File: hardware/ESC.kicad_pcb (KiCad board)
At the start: 4 copper layers, 52 x 25 mm, 89 parts, among them J1 +, J10 +, J2 -, J3 +, J4 +, J5 +, J6 +, J7 Conn_01x03, J8 +, J9 +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

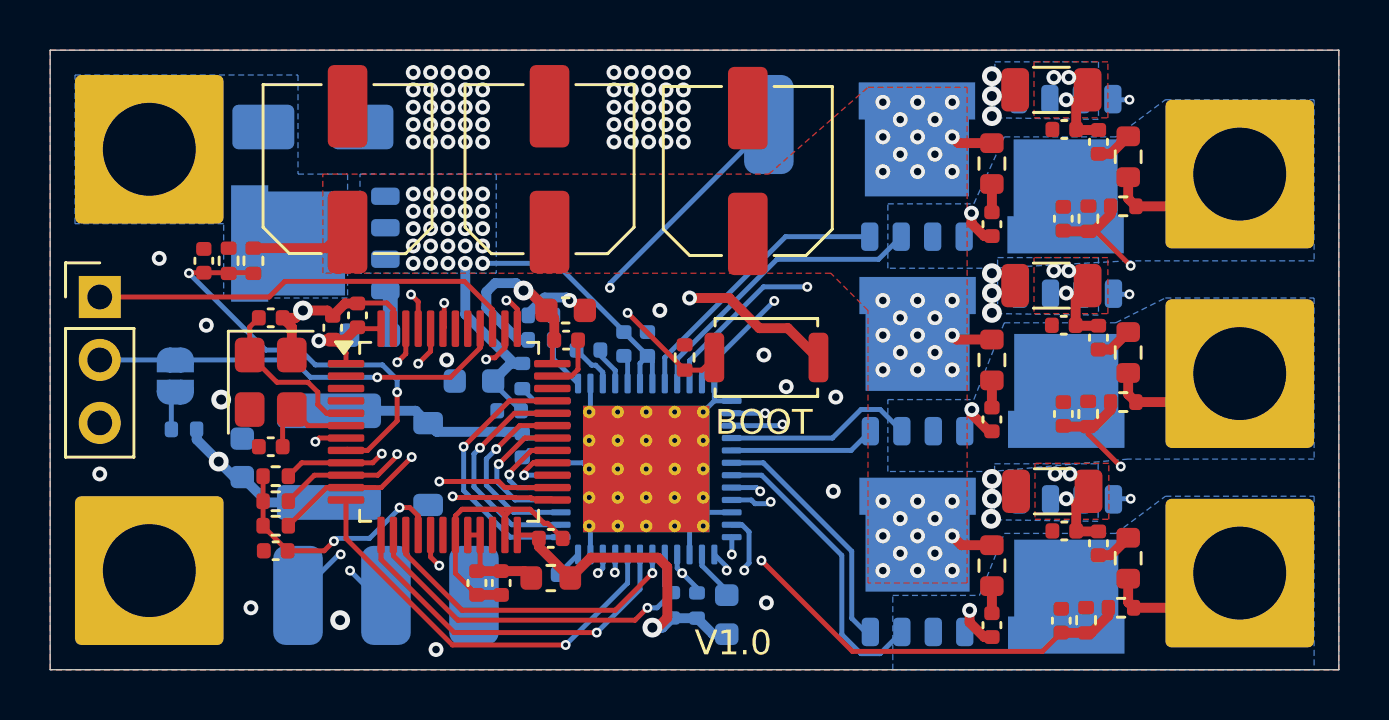
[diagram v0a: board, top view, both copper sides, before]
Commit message: increase via and trace size
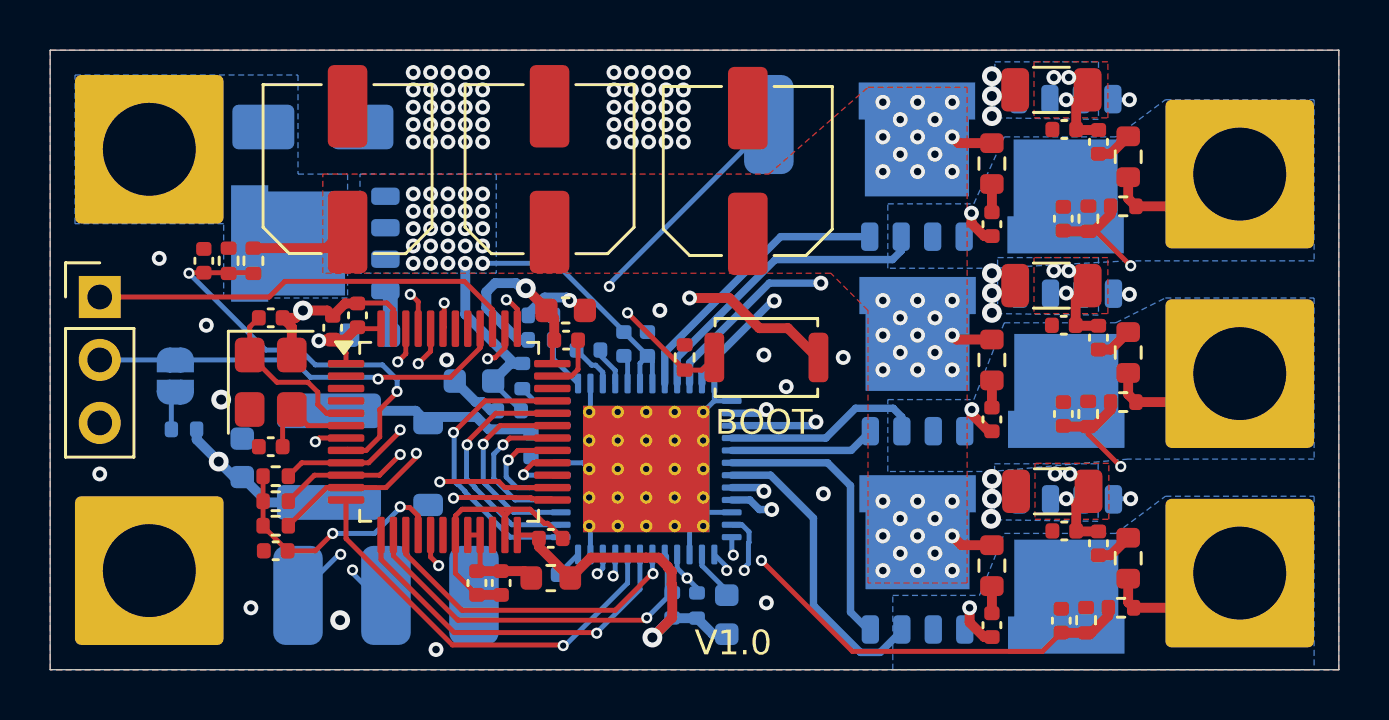
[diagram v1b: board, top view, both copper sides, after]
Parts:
- moved C7 0.35 mm to (157.4, 101.0)
- moved Q5 0.10 mm to (173.0, 105.7)
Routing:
- net /GLC: track 18.2 -> 21.0 mm
- net GND: track 46.6 -> 48.8 mm
- net /SPC: track 19.2 -> 17.0 mm
- net /GHC: track 10.1 -> 11.4 mm
- net /INHA: track 10.8 -> 11.7 mm
- net /SPA: track 23.4 -> 22.5 mm
- net +3.3V: track 51.7 -> 52.5 mm
- net /INLA: track 9.31 -> 10.00 mm
- net /INLB: track 6.22 -> 6.83 mm
- net /BGND: track 9.41 -> 10.0 mm
- net /INHB: track 7.74 -> 8.30 mm

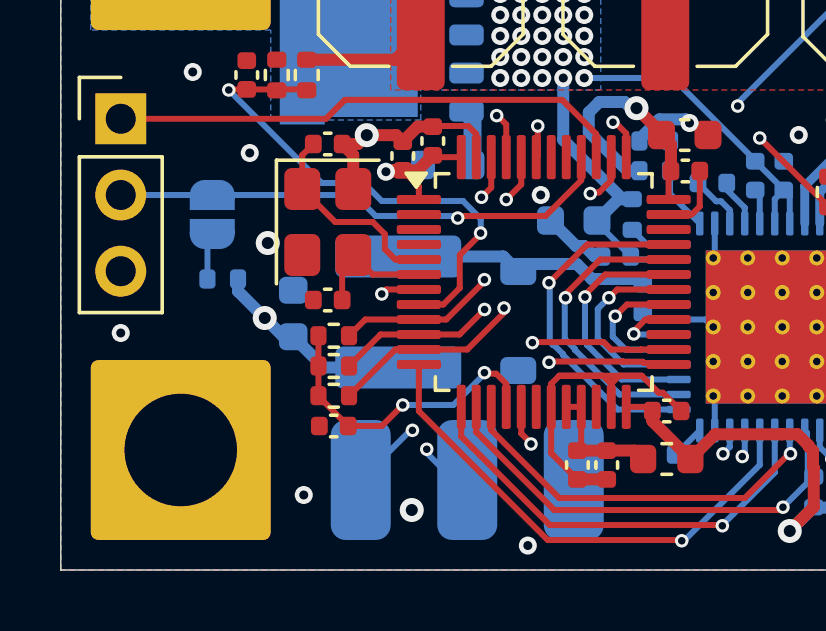
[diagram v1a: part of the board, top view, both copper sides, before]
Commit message: changed inductor size
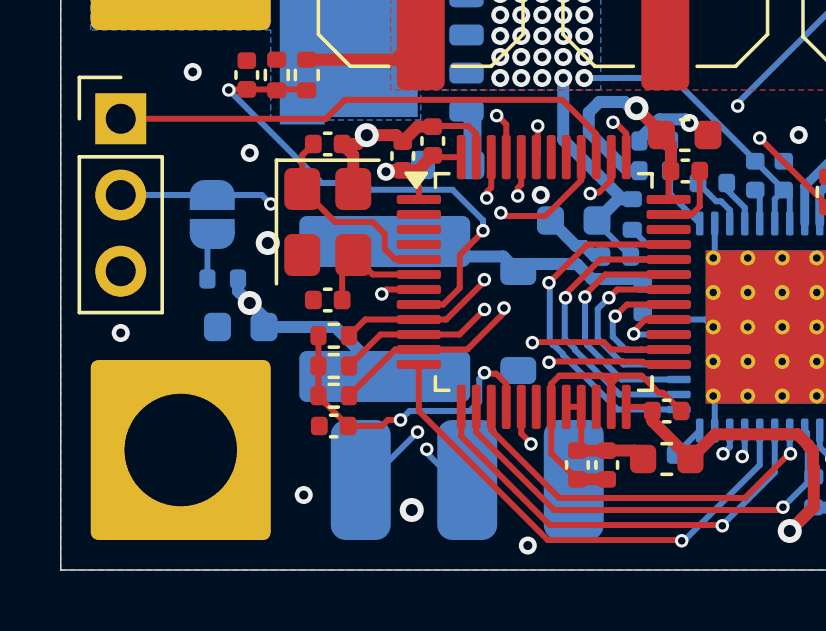
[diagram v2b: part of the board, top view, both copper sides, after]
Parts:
- L1: footprint Inductor_SMD:L_APV_ANR5012 -> Inductor_SMD:L_APV_ANR6020
- moved C8 1.81 mm to (144.0, 101.9), turned to 180 degrees
- moved L1 0.46 mm to (148.8, 101.3)
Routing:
- net /DIR: track 17.0 -> 16.9 mm, vias 1 -> 2
